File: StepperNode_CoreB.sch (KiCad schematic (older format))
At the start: 1 part

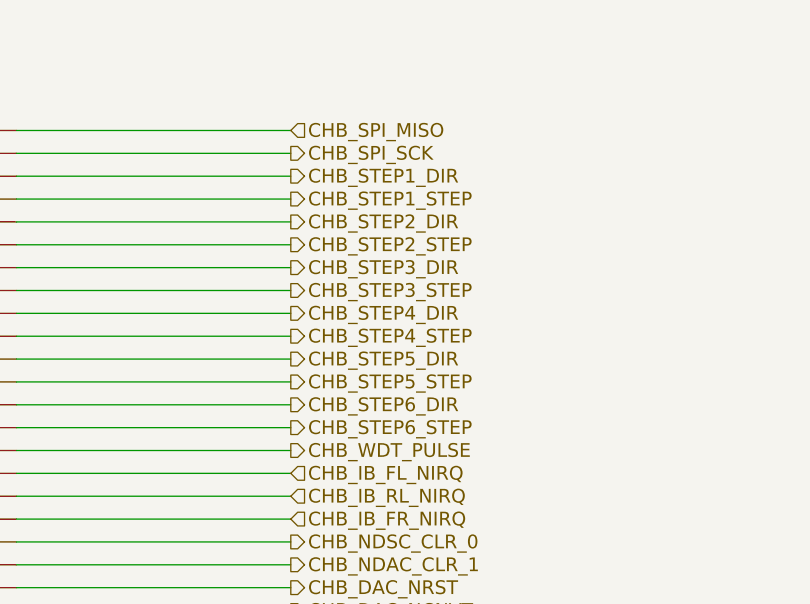
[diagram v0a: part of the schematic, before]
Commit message: Remove Gimbal Functions
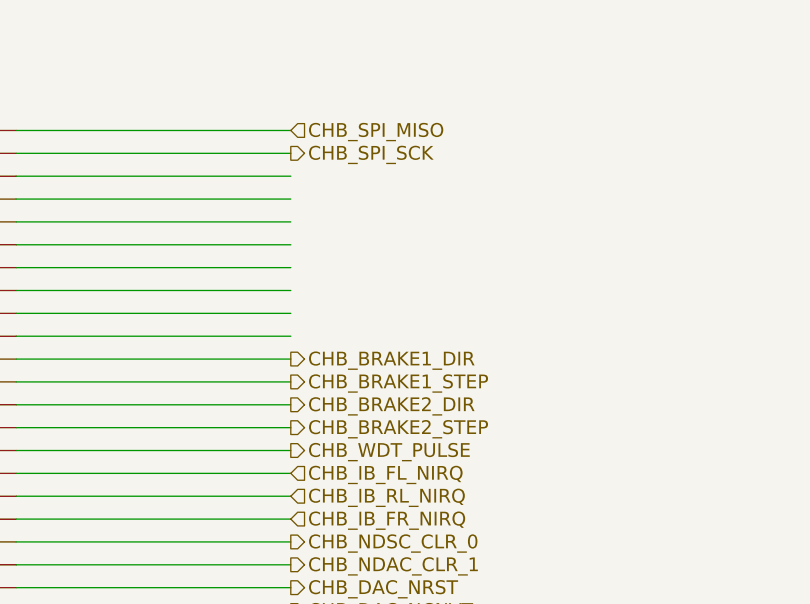
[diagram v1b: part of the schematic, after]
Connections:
- net labels added: CHB_BRAKE1_DIR, CHB_BRAKE1_STEP, CHB_BRAKE2_DIR, CHB_BRAKE2_STEP
- net labels removed: CHB_STEP1_DIR, CHB_STEP1_STEP, CHB_STEP2_DIR, CHB_STEP2_STEP, CHB_STEP3_DIR, CHB_STEP3_STEP, CHB_STEP4_DIR, CHB_STEP4_STEP, CHB_STEP5_DIR, CHB_STEP5_STEP, CHB_STEP6_DIR, CHB_STEP6_STEP
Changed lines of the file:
@@
 $Descr A3 16535 11693
 encoding utf-8
-Sheet 7 17
+Sheet 15 15
 Title "Core Interface - Channel B"
 Date ""
@@
 Text HLabel 10100 6100 2    60   Output ~ 0
 CHB_DAC_NCNVT
-Text HLabel 10100 4200 2    60   Output ~ 0
-CHB_STEP1_DIR
-Text HLabel 10100 4300 2    60   Output ~ 0
-CHB_STEP1_STEP
-Text HLabel 10100 4400 2    60   Output ~ 0
-CHB_STEP2_DIR
-Text HLabel 10100 4500 2    60   Output ~ 0
-CHB_STEP2_STEP
-Text HLabel 10100 4600 2    60   Output ~ 0
-CHB_STEP3_DIR
-Text HLabel 10100 4700 2    60   Output ~ 0
-CHB_STEP3_STEP
-Text HLabel 10100 4800 2    60   Output ~ 0
-CHB_STEP4_DIR
-Text HLabel 10100 4900 2    60   Output ~ 0
-CHB_STEP4_STEP
 Text HLabel 10100 5000 2    60   Output ~ 0
-CHB_STEP5_DIR
+CHB_BRAKE1_DIR
 Text HLabel 10100 5100 2    60   Output ~ 0
-CHB_STEP5_STEP
+CHB_BRAKE1_STEP
 Text HLabel 10100 5200 2    60   Output ~ 0
-CHB_STEP6_DIR
+CHB_BRAKE2_DIR
 Text HLabel 10100 5300 2    60   Output ~ 0
-CHB_STEP6_STEP
+CHB_BRAKE2_STEP
 Text HLabel 10100 5400 2    60   Output ~ 0
 CHB_WDT_PULSE

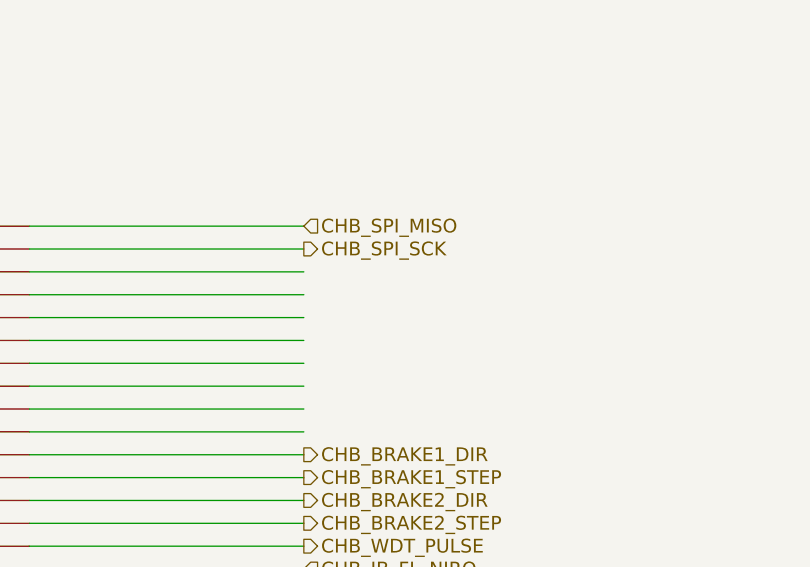
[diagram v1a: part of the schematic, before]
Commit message: Update DAC's and routed gimbal position to MCU direct.
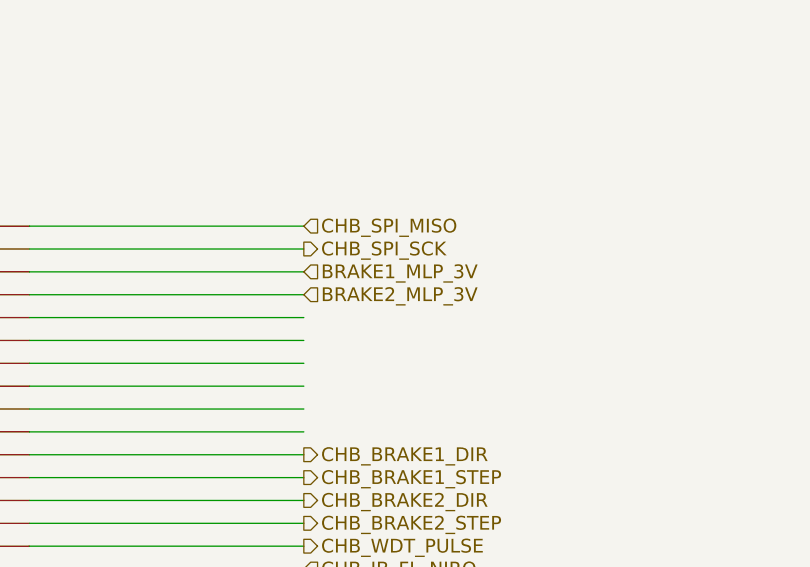
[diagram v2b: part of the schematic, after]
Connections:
- net labels added: BRAKE1_MLP_3V, BRAKE2_MLP_3V
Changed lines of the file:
@@
 Text Notes 11950 10500 0    60   ~ 0
 Original Author: SafetyLok
+Text HLabel 10100 4200 2    60   Input ~ 0
+BRAKE1_MLP_3V
+Text HLabel 10100 4300 2    60   Input ~ 0
+BRAKE2_MLP_3V
 $EndSCHEMATC

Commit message: First Revision -
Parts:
- gave numbers to parts that had none: 1
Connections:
- net labels added: +24V_B, +3V3_B, +5V_B, GNDA, IB_FL_RX_3V, IB_FL_TX, IB_FR_RX_3V, IB_FR_TX, IB_RL_RX_3V, IB_RL_TX
- net labels removed: +24V_A, +3V3_A, +5V_A, CHB_IB_FL_NCS, CHB_IB_FL_NIRQ, CHB_IB_FR_NCS, CHB_IB_FR_NIRQ, CHB_IB_RL_NCS, CHB_IB_RL_NIRQ, CHB_SPI_MISO, CHB_SPI_MOSI, CHB_SPI_SCK
- wire segments 40 -> 32
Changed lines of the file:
@@
 $EndDescr
 $Comp
-L NODE_CORE_CONNECTOR-RESCUE-rloopStepperNode A?
+L NODE_CORE_CONNECTOR-RESCUE-rloopStepperNode A2
 U 1 1 575E045E
 P 8150 5000
-F 0 "A?" H 8600 6400 60  0000 C CNN
+F 0 "A2" H 8600 6400 60  0000 C CNN
 F 1 "NODE_CORE_CONNECTOR" H 8850 3450 60  0000 C CNN
 F 2 "" H 8150 5000 60  0000 C CNN
@@
 Text HLabel 10100 6000 2    60   Output ~ 0
 CHB_DAC_NRST
-Text HLabel 6200 5500 0    60   Input ~ 0
+Text HLabel 6200 5900 0    60   Input ~ 0
 CHB_DAC_NDATA_AVAIL
 Text HLabel 10100 6100 2    60   Output ~ 0
@@
 Text HLabel 10100 5400 2    60   Output ~ 0
 CHB_WDT_PULSE
-Text HLabel 10100 5500 2    60   Input ~ 0
-CHB_IB_FL_NIRQ
-Text HLabel 10100 5600 2    60   Input ~ 0
-CHB_IB_RL_NIRQ
-Text HLabel 10100 5700 2    60   Input ~ 0
-CHB_IB_FR_NIRQ
-Text HLabel 6200 5100 0    60   Output ~ 0
-CHB_IB_RL_NCS
-Text HLabel 6200 5200 0    60   Output ~ 0
-CHB_IB_FR_NCS
-Text HLabel 6200 5000 0    60   Output ~ 0
-CHB_IB_FL_NCS
-Text HLabel 6200 5900 0    60   Output ~ 0
-CHB_SPI_MOSI
-Text HLabel 6200 5600 0    60   Output ~ 0
+Text HLabel 6200 5400 0    60   Output ~ 0
 CHB_AUXPROP_DIR
-Text HLabel 6200 5700 0    60   Input ~ 0
-PUSH_INTLK_A
-Text HLabel 6200 5800 0    60   Input ~ 0
-PUSH_INTLK_B
+Text HLabel 6200 5200 0    60   Input ~ 0
+CHB_ACCEL1_NINT
 Text HLabel 6200 5300 0    60   Input ~ 0
-CHB_ACCEL1_NINT
-Text HLabel 6200 5400 0    60   Input ~ 0
 CHB_ACCEL2_NINT
-$Comp
-L +3V3_A #PWR?
-U 1 1 575E0483
-P 8400 3450
-F 0 "#PWR?" H 8400 3300 50  0001 C CNN
-F 1 "+3V3_A" H 8400 3590 50  0000 C CNN
-F 2 "" H 8400 3450 60  0000 C CNN
-F 3 "" H 8400 3450 60  0000 C CNN
-	1    8400 3450
-	1    0    0    -1
-$EndComp
-$Comp
-L +5V_A #PWR?
-U 1 1 575E0489
-P 8200 3200
-F 0 "#PWR?" H 8200 3050 50  0001 C CNN
-F 1 "+5V_A" H 8200 3340 50  0000 C CNN
-F 2 "" H 8200 3200 60  0000 C CNN
-F 3 "" H 8200 3200 60  0000 C CNN
-	1    8200 3200
-	1    0    0    -1
-$EndComp
-$Comp
-L +24V_A #PWR?
-U 1 1 575E048F
-P 8000 3000
-F 0 "#PWR?" H 8000 2850 50  0001 C CNN
-F 1 "+24V_A" H 8000 3140 50  0000 C CNN
-F 2 "" H 8000 3000 60  0000 C CNN
-F 3 "" H 8000 3000 60  0000 C CNN
-	1    8000 3000
-	1    0    0    -1
-$EndComp
 Wire Wire Line
 	8000 3000 8000 3450
@@
 Wire Wire Line
 	8300 3450 8400 3450
-$Comp
-L GNDD #PWR?
-U 1 1 575E049A
-P 8250 6700
-F 0 "#PWR?" H 8250 6450 50  0001 C CNN
-F 1 "GNDD" H 8250 6550 50  0000 C CNN
-F 2 "" H 8250 6700 50  0000 C CNN
-F 3 "" H 8250 6700 50  0000 C CNN
-	1    8250 6700
-	1    0    0    -1
-$EndComp
-Wire Wire Line
-	8050 6700 8250 6700
 Wire Wire Line
 	7400 4800 6200 4800
@@
 	7400 5900 6200 5900
 Wire Wire Line
-	10100 4000 8900 4000
-Wire Wire Line
-	10100 4100 8900 4100
-Text HLabel 10100 4000 2    60   Input ~ 0
-CHB_SPI_MISO
-Text HLabel 10100 4100 2    60   Output ~ 0
-CHB_SPI_SCK
-Wire Wire Line
 	10100 4200 8900 4200
 Wire Wire Line
 	10100 4300 8900 4300
-Wire Wire Line
-	10100 4400 8900 4400
-Wire Wire Line
-	10100 4500 8900 4500
-Wire Wire Line
-	10100 4600 8900 4600
-Wire Wire Line
-	10100 4700 8900 4700
-Wire Wire Line
-	10100 4800 8900 4800
-Wire Wire Line
-	10100 4900 8900 4900
 Wire Wire Line
 	10100 5000 8900 5000
@@
 Wire Wire Line
 	10100 5600 8900 5600
-Wire Wire Line
-	10100 5700 8900 5700
 Wire Wire Line
 	10100 5100 8900 5100
@@
 Text HLabel 10100 4300 2    60   Input ~ 0
 BRAKE2_MLP_3V
+$Comp
+L GNDD #PWR204
+U 1 1 576221C2
+P 8050 6700
+F 0 "#PWR204" H 8050 6450 50  0001 C CNN
+F 1 "GNDD" H 8050 6550 50  0000 C CNN
+F 2 "" H 8050 6700 50  0000 C CNN
+F 3 "" H 8050 6700 50  0000 C CNN
+	1    8050 6700
+	1    0    0    -1
+$EndComp
+$Comp
+L GNDA #PWR206
+U 1 1 576221C8
+P 8250 6750
+F 0 "#PWR206" H 8250 6500 50  0001 C CNN
+F 1 "GNDA" H 8250 6600 50  0000 C CNN
+F 2 "" H 8250 6750 50  0000 C CNN
+F 3 "" H 8250 6750 50  0000 C CNN
+	1    8250 6750
+	1    0    0    -1
+$EndComp
+Wire Wire Line
+	8250 6700 8250 6750
+Wire Wire Line
+	8050 6700 8150 6700
+Text HLabel 6200 5100 0    60   Output ~ 0
+IB_FL_TX
+Text HLabel 6200 5000 0    60   Input ~ 0
+IB_FL_RX_3V
+Text HLabel 10100 5500 2    60   Input ~ 0
+PUSH_INTLK_A
+Text HLabel 10100 5600 2    60   Input ~ 0
+PUSH_INTLK_B
+Text HLabel 6200 5800 0    60   Output ~ 0
+IB_RL_TX
+Text HLabel 6200 5700 0    60   Input ~ 0
+IB_RL_RX_3V
+Text HLabel 6200 5600 0    60   Output ~ 0
+IB_FR_TX
+Text HLabel 6200 5500 0    60   Input ~ 0
+IB_FR_RX_3V
+$Comp
+L +3V3_B #PWR207
+U 1 1 57671EAB
+P 8400 3450
+F 0 "#PWR207" H 8400 3300 50  0001 C CNN
+F 1 "+3V3_B" H 8400 3590 50  0000 C CNN
+F 2 "" H 8400 3450 60  0000 C CNN
+F 3 "" H 8400 3450 60  0000 C CNN
+	1    8400 3450
+	1    0    0    -1
+$EndComp
+$Comp
+L +5V_B #PWR205
+U 1 1 57671EC2
+P 8200 3200
+F 0 "#PWR205" H 8200 3050 50  0001 C CNN
+F 1 "+5V_B" H 8200 3340 50  0000 C CNN
+F 2 "" H 8200 3200 60  0000 C CNN
+F 3 "" H 8200 3200 60  0000 C CNN
+	1    8200 3200
+	1    0    0    -1
+$EndComp
+$Comp
+L +24V_B #PWR203
+U 1 1 57671ED8
+P 8000 3000
+F 0 "#PWR203" H 8000 2850 50  0001 C CNN
+F 1 "+24V_B" H 8000 3140 50  0000 C CNN
+F 2 "" H 8000 3000 60  0000 C CNN
+F 3 "" H 8000 3000 60  0000 C CNN
+	1    8000 3000
+	1    0    0    -1
+$EndComp
 $EndSCHEMATC

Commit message: Fix most ERC warnings (non-connected pins, etc)
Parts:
- A2: symbol NODE_CORE_CONNECTOR-RESCUE-rloopStepperNode -> NODE_CORE_CONNECTOR
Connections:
- net CHB_I2C_SCL: now also A2.T29 (I2C_SCL); no longer A2.~ (ID8)
- net CHB_I2C_SDA: now also A2.T30 (I2C_SDA); no longer A2.~ (ID8)
- no-connect marks 0 -> 10
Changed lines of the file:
@@
 $EndDescr
 $Comp
-L NODE_CORE_CONNECTOR-RESCUE-rloopStepperNode A2
+L NODE_CORE_CONNECTOR A2
 U 1 1 575E045E
 P 8150 5000
@@
 BRAKE2_MLP_3V
 $Comp
-L GNDD #PWR204
+L GNDD #PWR0214
 U 1 1 576221C2
 P 8050 6700
-F 0 "#PWR204" H 8050 6450 50  0001 C CNN
+F 0 "#PWR0214" H 8050 6450 50  0001 C CNN
 F 1 "GNDD" H 8050 6550 50  0000 C CNN
 F 2 "" H 8050 6700 50  0000 C CNN
@@
 $EndComp
 $Comp
-L GNDA #PWR206
+L GNDA #PWR0215
 U 1 1 576221C8
 P 8250 6750
-F 0 "#PWR206" H 8250 6500 50  0001 C CNN
+F 0 "#PWR0215" H 8250 6500 50  0001 C CNN
 F 1 "GNDA" H 8250 6600 50  0000 C CNN
 F 2 "" H 8250 6750 50  0000 C CNN
@@
 IB_FR_RX_3V
 $Comp
-L +3V3_B #PWR207
+L +3V3_B #PWR0216
 U 1 1 57671EAB
 P 8400 3450
-F 0 "#PWR207" H 8400 3300 50  0001 C CNN
+F 0 "#PWR0216" H 8400 3300 50  0001 C CNN
 F 1 "+3V3_B" H 8400 3590 50  0000 C CNN
 F 2 "" H 8400 3450 60  0000 C CNN
@@
 $EndComp
 $Comp
-L +5V_B #PWR205
+L +5V_B #PWR0217
 U 1 1 57671EC2
 P 8200 3200
-F 0 "#PWR205" H 8200 3050 50  0001 C CNN
+F 0 "#PWR0217" H 8200 3050 50  0001 C CNN
 F 1 "+5V_B" H 8200 3340 50  0000 C CNN
 F 2 "" H 8200 3200 60  0000 C CNN
@@
 $EndComp
 $Comp
-L +24V_B #PWR203
+L +24V_B #PWR0218
 U 1 1 57671ED8
 P 8000 3000
-F 0 "#PWR203" H 8000 2850 50  0001 C CNN
+F 0 "#PWR0218" H 8000 2850 50  0001 C CNN
 F 1 "+24V_B" H 8000 3140 50  0000 C CNN
 F 2 "" H 8000 3000 60  0000 C CNN
@@
 	1    0    0    -1
 $EndComp
+NoConn ~ 8900 4000
+NoConn ~ 8900 4100
+NoConn ~ 8900 4400
+NoConn ~ 8900 4500
+NoConn ~ 8900 4600
+NoConn ~ 8900 4700
+NoConn ~ 8900 4800
+NoConn ~ 8900 4900
+NoConn ~ 8900 5700
+NoConn ~ 8900 6200
 $EndSCHEMATC

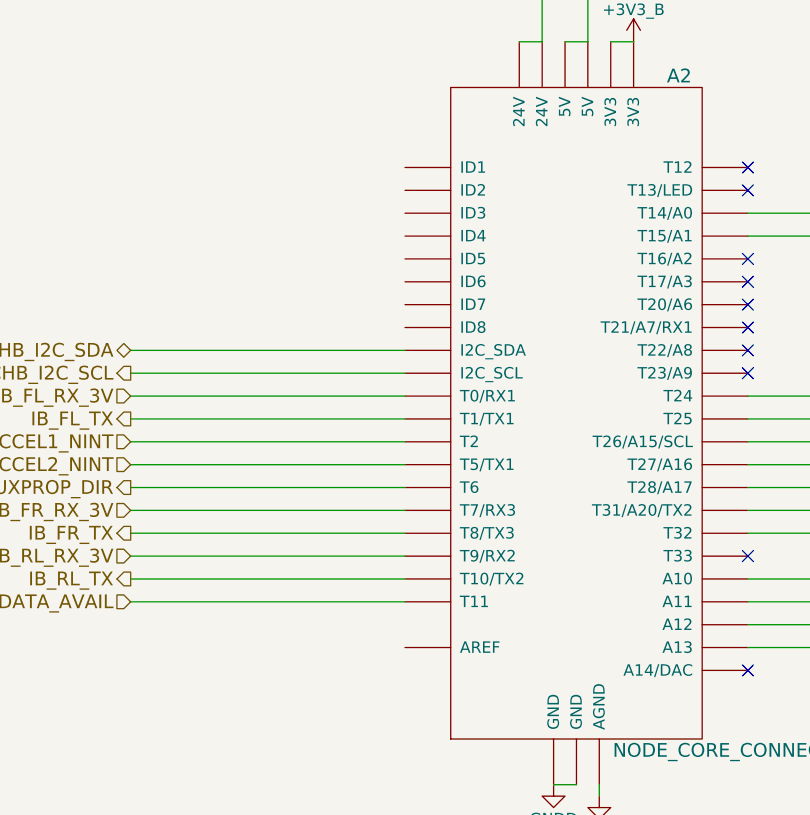
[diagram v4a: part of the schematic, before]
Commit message: Fix further ERC warnings
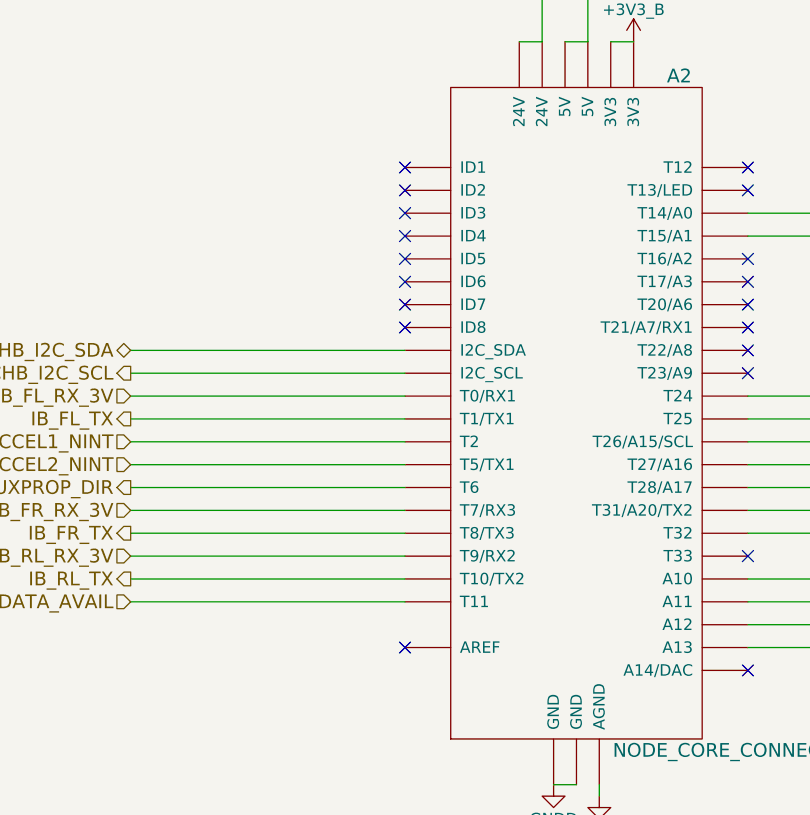
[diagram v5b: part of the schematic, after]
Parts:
- A2: footprint (none) -> footprints:NODECORE
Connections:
- no-connect marks 10 -> 19
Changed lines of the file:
@@
 F 0 "A2" H 8600 6400 60  0000 C CNN
 F 1 "NODE_CORE_CONNECTOR" H 8850 3450 60  0000 C CNN
-F 2 "" H 8150 5000 60  0000 C CNN
+F 2 "footprints:NODECORE" H 8150 5000 60  0001 C CNN
 F 3 "" H 8150 5000 60  0000 C CNN
 	1    8150 5000
@@
 NoConn ~ 8900 5700
 NoConn ~ 8900 6200
+NoConn ~ 7400 4000
+NoConn ~ 7400 4100
+NoConn ~ 7400 4200
+NoConn ~ 7400 4300
+NoConn ~ 7400 4400
+NoConn ~ 7400 4500
+NoConn ~ 7400 4600
+NoConn ~ 7400 4700
+NoConn ~ 7400 6100
 $EndSCHEMATC

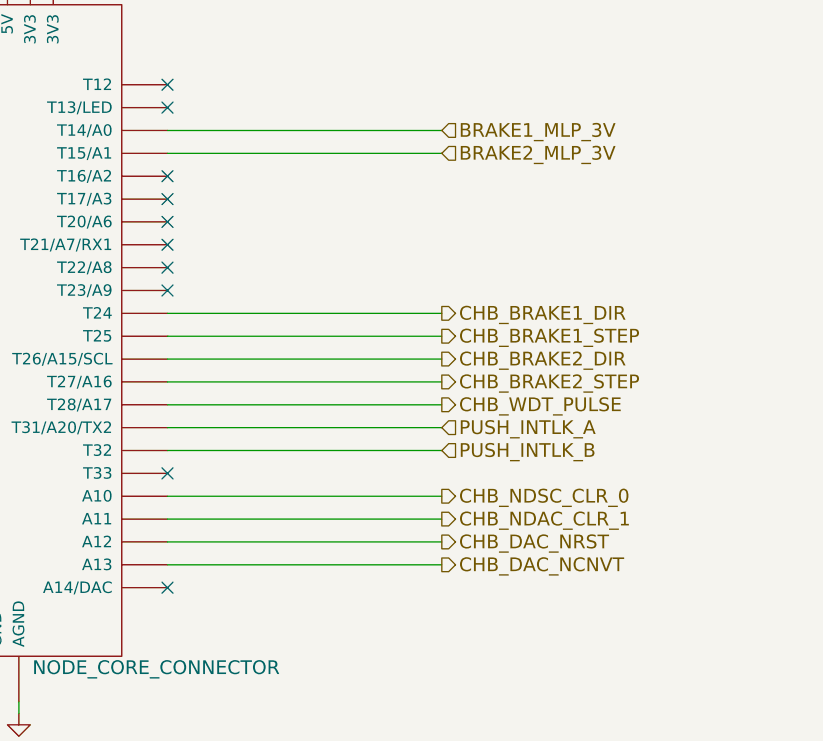
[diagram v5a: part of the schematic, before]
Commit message: Update Teensy IO and place isolation amp.
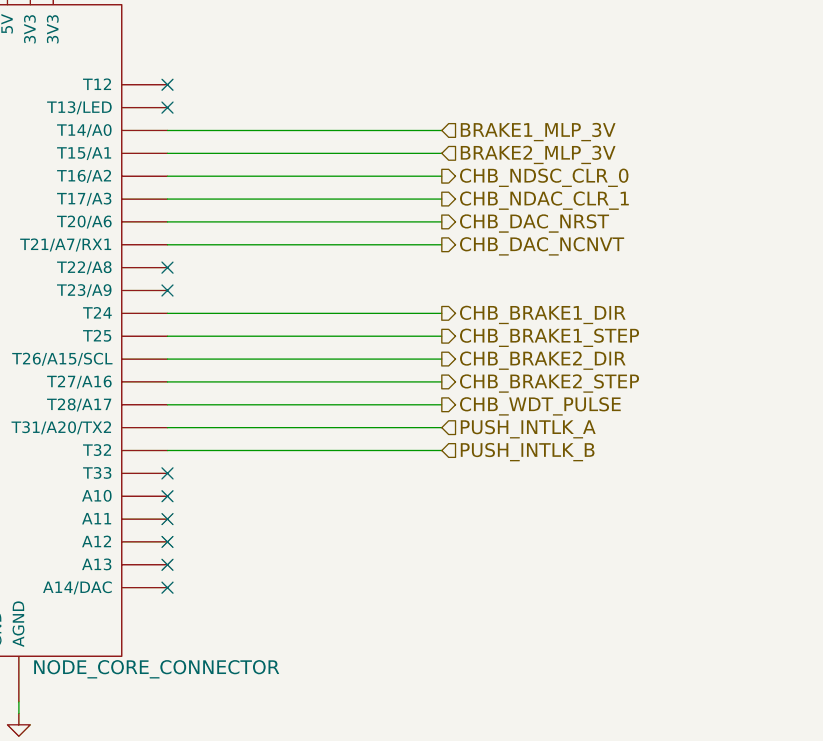
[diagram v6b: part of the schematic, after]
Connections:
- net CHB_DAC_NCNVT: now also A2.T21 (T21/A7/RX1); no longer A2.A13
- net CHB_DAC_NRST: now also A2.T20 (T20/A6); no longer A2.A12
- net CHB_NDAC_CLR_1: now also A2.T17 (T17/A3); no longer A2.A11
- net CHB_NDSC_CLR_0: now also A2.T16 (T16/A2); no longer A2.A10
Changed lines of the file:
@@
 	1    0    0    -1
 $EndComp
-Text HLabel 10100 5800 2    60   Output ~ 0
-CHB_NDSC_CLR_0
-Text HLabel 10100 5900 2    60   Output ~ 0
-CHB_NDAC_CLR_1
-Text HLabel 10100 6000 2    60   Output ~ 0
-CHB_DAC_NRST
 Text HLabel 6200 5900 0    60   Input ~ 0
 CHB_DAC_NDATA_AVAIL
-Text HLabel 10100 6100 2    60   Output ~ 0
-CHB_DAC_NCNVT
 Text HLabel 10100 5000 2    60   Output ~ 0
 CHB_BRAKE1_DIR
@@
 Wire Wire Line
 	10100 5400 8900 5400
-Wire Wire Line
-	10100 5900 8900 5900
-Wire Wire Line
-	10100 6000 8900 6000
-Wire Wire Line
-	10100 6100 8900 6100
-Wire Wire Line
-	10100 5800 8900 5800
 Wire Wire Line
 	7400 5300 6200 5300
@@
 NoConn ~ 8900 4000
 NoConn ~ 8900 4100
-NoConn ~ 8900 4400
-NoConn ~ 8900 4500
-NoConn ~ 8900 4600
-NoConn ~ 8900 4700
 NoConn ~ 8900 4800
 NoConn ~ 8900 4900
@@
 NoConn ~ 7400 4700
 NoConn ~ 7400 6100
+Text HLabel 10100 4400 2    60   Output ~ 0
+CHB_NDSC_CLR_0
+Text HLabel 10100 4500 2    60   Output ~ 0
+CHB_NDAC_CLR_1
+Text HLabel 10100 4600 2    60   Output ~ 0
+CHB_DAC_NRST
+Text HLabel 10100 4700 2    60   Output ~ 0
+CHB_DAC_NCNVT
+Wire Wire Line
+	10100 4500 8900 4500
+Wire Wire Line
+	10100 4600 8900 4600
+Wire Wire Line
+	10100 4700 8900 4700
+Wire Wire Line
+	10100 4400 8900 4400
+NoConn ~ 8900 5800
+NoConn ~ 8900 5900
+NoConn ~ 8900 6000
+NoConn ~ 8900 6100
 $EndSCHEMATC
